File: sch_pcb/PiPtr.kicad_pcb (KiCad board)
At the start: 2 copper layers, 101.6 x 152.4 mm, 318 parts, among them J101 GLOBAL LINK 1 LEFT, J102 GLOBAL LINK 1 RIGHT, J104 GLOBAL LINK 2 LEFT, J106 GLOBAL LINK 2 RIGHT, J107 RASPBERRY_PI, J111 FP_PIXEL, J112 AM2302, J113 I2C1_5V, J114 I2C0_3v3, J117 OLED, J201 TO_SOUNDCARD, J202 FROM_SOUNDCARD, J203 Radio Port, J204 DB9_FEMALE, J301 SPARE, J302 SPARE, J303 SPARE, J304 SPARE, J305 USER_GPIO, J306 SPARE, J307 SPARE, J308 SPARE, J309 SPARE, J310 SPARE, J311 SPARE, J312 USER_ADC, J313 SPARE, J314 SPARE, J315 12VDC_IN, J401 TO_SOUNDCARD, J402 FROM_SOUNDCARD, J403 Radio Port, J404 DB9_FEMALE, Q101 2N7000, Q102 2N7000, Q103 2N7000, Q104 2N7000, Q105 2N7000, Q201 2N7000, Q202 2N7000, Q203 2N7000, Q301 SPARE, Q302 SPARE, Q401 2N7000, Q402 2N7000, Q403 2N7000, U101 MCP23017, U102 IP4234CZ6, U103 MCP4351, U104 74HC138, U105 74LVC1G125, U106 MCP4351, U107 MCP4351, U108 IP4234CZ6, U109 IP4234CZ6, U110 CD4050B, U201 MCP6004N, U202 74LVC1G3157, U203 74LVC1G3157, U204 74LVC4066, U205 MCP6004N, U206 74LVC1G3157, U207 MCP6S26, U301 MCP23017, U302 SPARE, U303 SPARE, U304 MCP3008, U305 MCP1703A-2502/MB, U306 TPS54302, U401 MCP6004N, U402 74LVC1G3157, U403 74LVC1G3157, U404 74LVC4066, U405 MCP6004N, U406 74LVC1G3157, U407 MCP6S26

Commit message: Updates based on emails
Disconnect SDO on PGAs
Add mounting holes 
More placement on PCB - for now, delete all 4xx sheet footprints.  Once channel 1 is placed, it will get copied to make channel 2.
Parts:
- removed C401, C402, C404, C408, C414, C415, C416, C418, C421, C423, C424, C425: 4.7u, lib:smd0603
- removed C403, C411, C413, C417, C419: 33p, lib:smd0603
- removed C405, C407, C420, C422: 0.1u, lib:smd0603
- removed C409, C410: 0.027u, lib:smd0603
- removed C412: 0.0039u, lib:smd0603
- removed C426, C427, C428, C429, C430, C431: 100p, lib:smd0603
- removed Q401, Q402, Q403: 2N7000, lib:SOT23
- removed R401, R410, R427, R436, R437, R440: 100k, lib:smd0603
- removed R402, R403, R408, R413, R430, R438, R439: 1k, lib:smd0603
- removed R404, R420, R431, R441, R442, R443: 20k, lib:smd0603
- removed R405, R406, R421, R422, R424, R425, R428, R429, R432, R433: 10k, lib:smd0603
- removed R407, R411, R434: 33, lib:smd0603
- removed R412, R415, R419, R426: 2k, lib:smd0603
- removed R414: 13k7, lib:smd0603
- removed R416, R418: 50k, lib:smd0603
- removed R417: 27k, lib:smd0603
- removed R423: 200k, lib:smd0603
- removed R435: 680, lib:smd0603
- removed TP401: TESTPOINT, lib:Wire_28AWG
- removed U401, U405: MCP6004N, lib:SOIC14
- removed U402, U403, U406: 74LVC1G3157, lib:SOT23-6
- removed U404: 74LVC4066, lib:SOIC14
- removed U407: MCP6S26, lib:SOIC14
- added MTG301: VAL**, lib:MTG_4_40, F.Cu at (59.7, 31.8)
- C311, C312, C313, C314, C315, C316, C317, C318: footprint lib:smd0805 -> lib:smd0603
- U301: moved to B.Cu
- moved U109 275.8 mm to (44.5, 190.5), turned to 90 degrees
- moved J113 262.8 mm to (25.4, 186.7)
- moved J114 262.8 mm to (41.9, 186.7)
- moved U108 254.6 mm to (27.9, 189.9), turned to 90 degrees
- moved TP104 246.7 mm to (24.1, 189.9)
- moved J102 231.8 mm to (39.4, 153.0)
- moved TP105 230.1 mm to (40.6, 189.9)
- moved J101 226.7 mm to (40.0, 142.9)
- moved U104 224.8 mm to (23.5, 149.2)
- moved U110 224.8 mm to (23.5, 157.5)
- moved C209 224.7 mm to (19.7, 109.9)
- moved C211 224.7 mm to (19.7, 119.4)
- moved C213 224.7 mm to (19.7, 117.5)
- moved R214 224.7 mm to (19.7, 108.0)
- moved R216 224.7 mm to (19.7, 111.8)
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
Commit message: Add files via upload
Fix missing pin numbers on opamps
Change two 4.7uF caps in parallel to 10uF/0805.  This will save 6 caps and will handle capacitance loss due to DC bias better
Change 2 22uF caps to 4 10uF caps to get rid of an extra BOM line item
More work on placement.  The channel now fits in the space allocated to it. 
Connectors need to be revisited - GPIO and soundcard
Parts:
- removed C215, C218, C224, C406: 4.7u, lib:smd0603
- removed J403: Radio Port, lib:RibbonHeader2x5
- added MTG302: VAL**, lib:MTG_4_40, F.Cu at (59.4, 176.8)
- added MTG303: VAL**, lib:MTG_4_40, F.Cu at (154.2, 177.0)
- added MTG304: VAL**, lib:MTG_4_40, F.Cu at (153.9, 31.5)
- U301: moved to F.Cu
- moved R122 160.1 mm to (178.3, 123.7)
- moved J401 152.5 mm to (112.5, 210.3), turned to 180 degrees
- moved J402 149.9 mm to (129.3, 211.3), turned to 180 degrees
- moved J404 108.3 mm to (113.5, 43.9)
- moved U107 106.7 mm to (174.2, 80.3), turned to 270 degrees
- moved J311 95.6 mm to (83.8, 90.2), turned to 90 degrees
- moved R227 93.8 mm to (89.4, 52.8)
- moved J102 93.2 mm to (130.3, 173.5), turned to 180 degrees
- moved J308 83.8 mm to (96.0, 90.7), turned to 90 degrees
- moved R203 75.1 mm to (82.3, 106.4)
- moved R204 71.9 mm to (82.0, 109.0)
- moved C216 71.3 mm to (89.4, 51.3)
- moved U110 69.6 mm to (81.8, 119.4)
- moved C220 68.8 mm to (77.2, 68.6), turned to 180 degrees
- moved C211 67.8 mm to (80.8, 89.9), turned to 90 degrees
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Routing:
- net /CH1/TX_CTCSS: track 0.00 -> 45.7 mm
- net /CH1/TX_AUDIO: track 0.00 -> 21.9 mm
- net /CH1/PTT: track 0.00 -> 10.0 mm
- net /CH1/RX_COR: track 0.00 -> 9.77 mm
- net /CH1/RX_AUDIO: track 0.00 -> 9.67 mm
- net /CH1/RX_CTCSS: track 0.00 -> 9.41 mm
- net /CH1/VDDA_2: track 0.00 -> 5.85 mm
- net Net-(C214-Pad2): track 0.00 -> 5.70 mm
- net Net-(C219-Pad1): track 0.00 -> 5.56 mm
- net Net-(C217-Pad2): track 0.00 -> 5.33 mm
- net Net-(C203-Pad2): track 0.00 -> 5.33 mm
- net Net-(C223-Pad2): track 0.00 -> 5.31 mm
- net Net-(C225-Pad1): track 0.00 -> 5.20 mm
- net Net-(C219-Pad2): track 0.00 -> 4.85 mm
- net Net-(C203-Pad1): track 0.00 -> 3.91 mm
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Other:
- board text added: "ADC/GPIO"
- board text added: "CHAN 1"
- board text added: "CHAN 2"
- board text added: "Todo: Replace with Molex/JST"

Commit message: Add files via upload
Changed  user_adc connector to 2x7 (14-pin is a lot more common than 12-pin)
Changed user_gpio connector to 2 2x8 connectors.  1x20 takes too much linear space
First pass layout on the two audio channels.  Right now, board is 4-layer, 100x150mm.  May be able to knock down the 150mm dimension 
The link and soundcard connectors fit in a row across the front edge.
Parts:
- removed J312: USER_ADC, lib:pin_array_6x2
- removed TP101: TESTPOINT, lib:Wire_28AWG
- added C324: 10u, lib:smd0805, F.Cu at (89.2, 226.1)
- added C325: 10u, lib:smd0805, F.Cu at (93.2, 230.6)
- added C401: 4.7u, lib:smd0603, F.Cu at (125.7, 55.9)
- added C402: 4.7u, lib:smd0603, F.Cu at (102.9, 86.6)
- added C403: 33p, lib:smd0603, F.Cu at (106.4, 56.4)
- added C404: 4.7u, lib:smd0603, F.Cu at (107.7, 90.2)
- added C405: 0.1u, lib:smd0603, F.Cu at (109.2, 90.2)
- added C406: 4.7u, lib:smd0603, F.Cu at (119.6, 55.9)
- added C407: 0.1u, lib:smd0603, F.Cu at (124.7, 73.2)
- added C408: 4.7u, lib:smd0603, F.Cu at (124.7, 71.6)
- added C409: 0.027u, lib:smd0603, F.Cu at (114.6, 83.8)
- added C410: 0.027u, lib:smd0603, F.Cu at (108.7, 94.0)
- added C411: 33p, lib:smd0603, F.Cu at (120.1, 84.6)
- added C412: 0.0039u, lib:smd0603, F.Cu at (117.9, 97.5)
- added C413: 33p, lib:smd0603, F.Cu at (110.7, 84.6)
- added C414: 10u, lib:smd0805, F.Cu at (116.3, 56.4)
- added C416: 10u, lib:smd0805, F.Cu at (120.4, 69.8)
- added C417: 33p, lib:smd0603, F.Cu at (113.0, 54.9)
- added C419: 33p, lib:smd0603, F.Cu at (114.3, 68.6)
- added C420: 0.1u, lib:smd0603, F.Cu at (110.5, 67.1)
- added C421: 4.7u, lib:smd0603, F.Cu at (110.5, 68.6)
- added C422: 0.1u, lib:smd0603, F.Cu at (103.6, 94.0)
- added C423: 10u, lib:smd0805, F.Cu at (104.9, 68.2)
- added C425: 4.7u, lib:smd0603, F.Cu at (108.2, 68.6)
- added C426: 100p, lib:smd0603, F.Cu at (119.0, 48.3)
- added C427: 100p, lib:smd0603, F.Cu at (117.3, 48.3)
- added C428: 100p, lib:smd0603, F.Cu at (113.3, 48.3)
- added C429: 100p, lib:smd0603, F.Cu at (110.7, 48.3)
- added C430: 100p, lib:smd0603, F.Cu at (107.6, 48.3)
- added C431: 100p, lib:smd0603, F.Cu at (114.6, 48.3)
- added J403: Radio Port, lib:RibbonHeader2x5, F.Cu at (113.3, 36.8)
- added Q401: 2N7000, lib:SOT23, F.Cu at (100.6, 49.5)
- added Q402: 2N7000, lib:SOT23, F.Cu at (100.6, 65.3)
- added Q403: 2N7000, lib:SOT23, F.Cu at (100.6, 57.7)
- added R121: 10k, lib:smd0603, F.Cu at (115.7, 62.4)
- added R401: 100k, lib:smd0603, F.Cu at (125.7, 54.4)
- added R402: 1k, lib:smd0603, F.Cu at (125.7, 57.4)
- added R403: 1k, lib:smd0603, F.Cu at (102.1, 94.0)
- added R404: 20k, lib:smd0603, F.Cu at (100.3, 94.0)
- added R405: 10k, lib:smd0603, F.Cu at (106.4, 54.9)
- added R406: 10k, lib:smd0603, F.Cu at (106.4, 53.3)
- added R407: 33, lib:smd0603, F.Cu at (106.2, 90.2)
- added R408: 1k, lib:smd0603, F.Cu at (115.1, 74.7)
- added R410: 100k, lib:smd0603, F.Cu at (121.2, 54.4)
- added R411: 33, lib:smd0603, F.Cu at (124.7, 70.1)
- added R412: 2k, lib:smd0603, F.Cu at (115.1, 76.2)
- added R413: 1k, lib:smd0603, F.Cu at (119.6, 57.4)
- added R414: 13k7, lib:smd0603, F.Cu at (108.7, 92.5)
- added R415: 2k, lib:smd0603, F.Cu at (115.1, 77.7)
- added R416: 50k, lib:smd0603, F.Cu at (113.8, 96.8)
- added R417: 27k, lib:smd0603, F.Cu at (108.7, 95.5)
- added R418: 50k, lib:smd0603, F.Cu at (119.4, 97.5)
- added R419: 2k, lib:smd0603, F.Cu at (115.1, 79.0)
- added R420: 20k, lib:smd0603, F.Cu at (117.3, 71.6)
- added R421: 10k, lib:smd0603, F.Cu at (120.1, 86.1)
- added R422: 10k, lib:smd0603, F.Cu at (122.4, 85.3)
- added R423: 200k, lib:smd0603, F.Cu at (116.3, 97.5)
- added R424: 10k, lib:smd0603, F.Cu at (112.3, 84.6)
- added R425: 10k, lib:smd0603, F.Cu at (108.2, 87.9)
- added R426: 2k, lib:smd0603, F.Cu at (115.1, 80.5)
- added R427: 100k, lib:smd0603, F.Cu at (120.4, 71.4)
- added R428: 10k, lib:smd0603, F.Cu at (113.0, 56.4)
- added R429: 10k, lib:smd0603, F.Cu at (113.0, 53.3)
- added R430: 1k, lib:smd0603, F.Cu at (120.4, 68.3)
- added R431: 20k, lib:smd0603, F.Cu at (115.1, 70.9)
- added R432: 10k, lib:smd0603, F.Cu at (114.3, 67.1)
- added R433: 10k, lib:smd0603, F.Cu at (113.5, 70.9)
- added R434: 33, lib:smd0603, F.Cu at (110.5, 70.1)
- added R435: 680, lib:smd0603, F.Cu at (87.0, 220.9)
- added R436: 100k, lib:smd0603, F.Cu at (104.4, 70.9)
- added R437: 100k, lib:smd0603, F.Cu at (106.7, 68.6)
- added R438: 1k, lib:smd0603, F.Cu at (100.3, 53.3)
- added R439: 1k, lib:smd0603, F.Cu at (100.1, 62.5)
- added R440: 100k, lib:smd0603, F.Cu at (103.9, 64.9)
- added R441: 20k, lib:smd0603, F.Cu at (100.1, 61.0)
- added R442: 20k, lib:smd0603, F.Cu at (100.3, 54.9)
- added R443: 20k, lib:smd0603, F.Cu at (103.1, 68.6)
- added TP301: TESTPOINT, lib:Wire_28AWG, F.Cu at (91.2, 96.5)
- added TP302: TESTPOINT, lib:Wire_28AWG, F.Cu at (91.2, 98.6)
- added TP303: TESTPOINT, lib:Wire_28AWG, F.Cu at (91.2, 100.6)
- added TP304, TP305, TP306: TESTPOINT, lib:Wire_28AWG, F.Cu at (87.0, 220.9)
- added TP401: TESTPOINT, lib:Wire_28AWG, F.Cu at (104.4, 51.3)
- added U111: 74LV1T125, lib:SOT23-5, F.Cu at (62.7, 230.6)
- added U112: 74LV1T125, lib:SOT23-5, F.Cu at (56.1, 230.1)
- added U401: MCP6004N, lib:SOIC14, F.Cu at (114.6, 90.9)
- added U402: 74LVC1G3157, lib:SOT23-6, F.Cu at (106.9, 85.3)
- added U403: 74LVC1G3157, lib:SOT23-6, F.Cu at (102.6, 90.4)
- added U404: 74LVC4066, lib:SOIC14, F.Cu at (105.7, 78.2)
- added U405: MCP6004N, lib:SOIC14, F.Cu at (109.7, 61.5)
- added U406: 74LVC1G3157, lib:SOT23-6, F.Cu at (123.2, 97.5)
- added U407: MCP6S26, lib:SOIC14, F.Cu at (120.9, 78.7)
- C214, C216, C223: value 4.7u -> 10u; footprint lib:smd0603 -> lib:smd0805
- C322, C323: value 22u -> 10u
- J305: value USER_GPIO -> USER_GPIO_2; footprint lib:SIL-20 -> lib:RibbonHeader2x8
- J308: value SPARE -> USER_GPIO_1; footprint lib:SIL-3 -> lib:RibbonHeader2x8
- J311: value SPARE -> USER_ADC; footprint lib:SIL-3 -> lib:RibbonHeader2x7
- MTG301, MTG302, MTG303, MTG304: value VAL** -> MOUNTING_HOLE
- U105: value 74LVC1G125 -> 74LV1T125
- moved J313 305.0 mm to (12.7, 221.0)
- moved J302 297.2 mm to (12.7, 228.6)
- moved J314 292.4 mm to (12.7, 217.2)
- moved U302 280.3 mm to (34.3, 224.8)
- moved J111 246.0 mm to (34.3, 218.4)
- moved Q301 242.5 mm to (78.0, 227.1), turned to 0 degrees
- moved J303 236.7 mm to (75.4, 212.9)
- moved Q302 235.3 mm to (73.4, 227.1), turned to 0 degrees
- moved R306 232.0 mm to (87.0, 220.9), turned to 0 degrees
- moved J304 231.7 mm to (75.4, 215.9)
- moved R303 228.0 mm to (87.0, 220.9), turned to 0 degrees
- moved R305 227.0 mm to (87.0, 220.9), turned to 0 degrees
- moved U306 224.8 mm to (62.7, 223.5)
- moved R302 223.5 mm to (87.0, 220.9), turned to 0 degrees
- moved R307 222.8 mm to (87.0, 220.9), turned to 0 degrees
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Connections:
- J107 pad 10: /UINTB -> /UINTB_33
- J107 pad 8: /UINTA -> /UINTA_33
- J305 pad 1: GND -> Net-(J305-Pad1)
- J305 pad 10: Net-(J305-Pad10) -> GND
- J305 pad 11: GND -> Net-(J305-Pad11)
- J305 pad 12: Net-(J305-Pad12) -> GND
- J305 pad 14: Net-(J305-Pad14) -> GND
- J305 pad 16: Net-(J305-Pad16) -> GND
- J305 pad 4: Net-(J305-Pad4) -> GND
- J305 pad 6: Net-(J305-Pad6) -> GND
- J305 pad 8: Net-(J305-Pad8) -> GND
- J308 pad 2: Net-(J308-Pad2) -> GND
- J311 pad 1: Net-(J311-Pad1) -> /Spares, GPIO, and ADC/ADC0
- J311 pad 2: Net-(J311-Pad2) -> GND
- J311 pad 3: Net-(J311-Pad3) -> /Spares, GPIO, and ADC/ADC1
- U101 pad 8: Net-(TP101-Pad1) -> /~UINT_ENA
- U106 pad 1: Net-(J311-Pad3) -> Net-(TP306-Pad1)
- U106 pad 18: Net-(J308-Pad1) -> Net-(TP301-Pad1)
- U106 pad 19: Net-(J308-Pad2) -> Net-(TP302-Pad1)
- U106 pad 2: Net-(J311-Pad2) -> Net-(TP305-Pad1)
- U106 pad 20: Net-(J308-Pad3) -> Net-(TP303-Pad1)
- U106 pad 3: Net-(J311-Pad1) -> Net-(TP304-Pad1)
- U107 pad 15: Net-(R119-Pad1) -> Net-(R121-Pad1)
- U204 pad 10: Net-(R226-Pad2) -> Net-(R215-Pad2)
- U204 pad 12: /RX1_BUS3_EN -> /RX1_BUS1_EN
- U204 pad 13: /RX1_LOCAL_EN -> /RX1_BUS2_EN
- U204 pad 2: Net-(R212-Pad2) -> Net-(R219-Pad2)
- U204 pad 3: Net-(R215-Pad2) -> Net-(R226-Pad2)
- U204 pad 5: /RX1_BUS1_EN -> /RX1_BUS3_EN
- U204 pad 6: /RX1_BUS2_EN -> /RX1_LOCAL_EN
- U204 pad 9: Net-(R219-Pad2) -> Net-(R212-Pad2)
- U207 pad 12: MISO_5 -> (no net)
- U301 pad 1: Net-(J305-Pad3) -> Net-(J305-Pad1)
- U301 pad 19: /UINTB -> /UINTB_5
- U301 pad 2: Net-(J305-Pad4) -> Net-(J305-Pad3)
- U301 pad 20: /UINTA -> /UINTA_5
- U301 pad 21: Net-(J305-Pad12) -> Net-(J308-Pad1)
- U301 pad 22: Net-(J305-Pad13) -> Net-(J308-Pad3)
- U301 pad 23: Net-(J305-Pad14) -> Net-(J308-Pad5)
- U301 pad 24: Net-(J305-Pad15) -> Net-(J308-Pad7)
- U301 pad 25: Net-(J305-Pad16) -> Net-(J308-Pad9)
- U301 pad 26: Net-(J305-Pad17) -> Net-(J308-Pad11)
- U301 pad 27: Net-(J305-Pad18) -> Net-(J308-Pad13)
- U301 pad 28: Net-(J305-Pad19) -> Net-(J308-Pad15)
- U301 pad 4: Net-(J305-Pad6) -> Net-(J305-Pad7)
- U301 pad 5: Net-(J305-Pad7) -> Net-(J305-Pad9)
- U301 pad 6: Net-(J305-Pad8) -> Net-(J305-Pad11)
- U301 pad 7: Net-(J305-Pad9) -> Net-(J305-Pad13)
- U301 pad 8: Net-(J305-Pad10) -> Net-(J305-Pad15)
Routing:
- net +5V: track 0.00 -> 333.5 mm, vias 0 -> 21
- net SCLK_5: track 0.00 -> 123.5 mm, vias 0 -> 4
- net MISO_5: track 0.00 -> 118.2 mm, vias 0 -> 8
- net MOSI_5: track 0.00 -> 114.4 mm, vias 0 -> 6
- net GND: track 0.00 -> 78.7 mm, vias 0 -> 41
- net /CH2/RX_CTCSS: track 0.00 -> 64.5 mm, vias 0 -> 1
- net Net-(C403-Pad1): track 0.00 -> 63.3 mm, vias 0 -> 4
- net /CH1/RX_CTCSS: track 9.41 -> 64.5 mm, vias 0 -> 1
- net /PTT2D: track 0.00 -> 53.3 mm
- net /PTT1D: track 0.00 -> 53.3 mm
- net +2V5: track 0.00 -> 48.8 mm, vias 0 -> 34
- net Net-(U103-Pad12): track 0.00 -> 47.1 mm, vias 0 -> 2
- net /~CTCSS2: track 0.00 -> 46.4 mm
- net /~CTCSS1: track 0.00 -> 46.4 mm
- net /LINK2_AUD: track 0.00 -> 45.1 mm, vias 0 -> 2
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- added copper zone on In2.Cu, net +2V5
- added copper zone on In1.Cu, net GND
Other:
- board size 101.6 x 152.4 mm -> 105 x 150 mm
- copper layers 2 -> 4
- board text removed: "ADC/GPIO"
- board text removed: "Todo: Replace with Molex/JST"

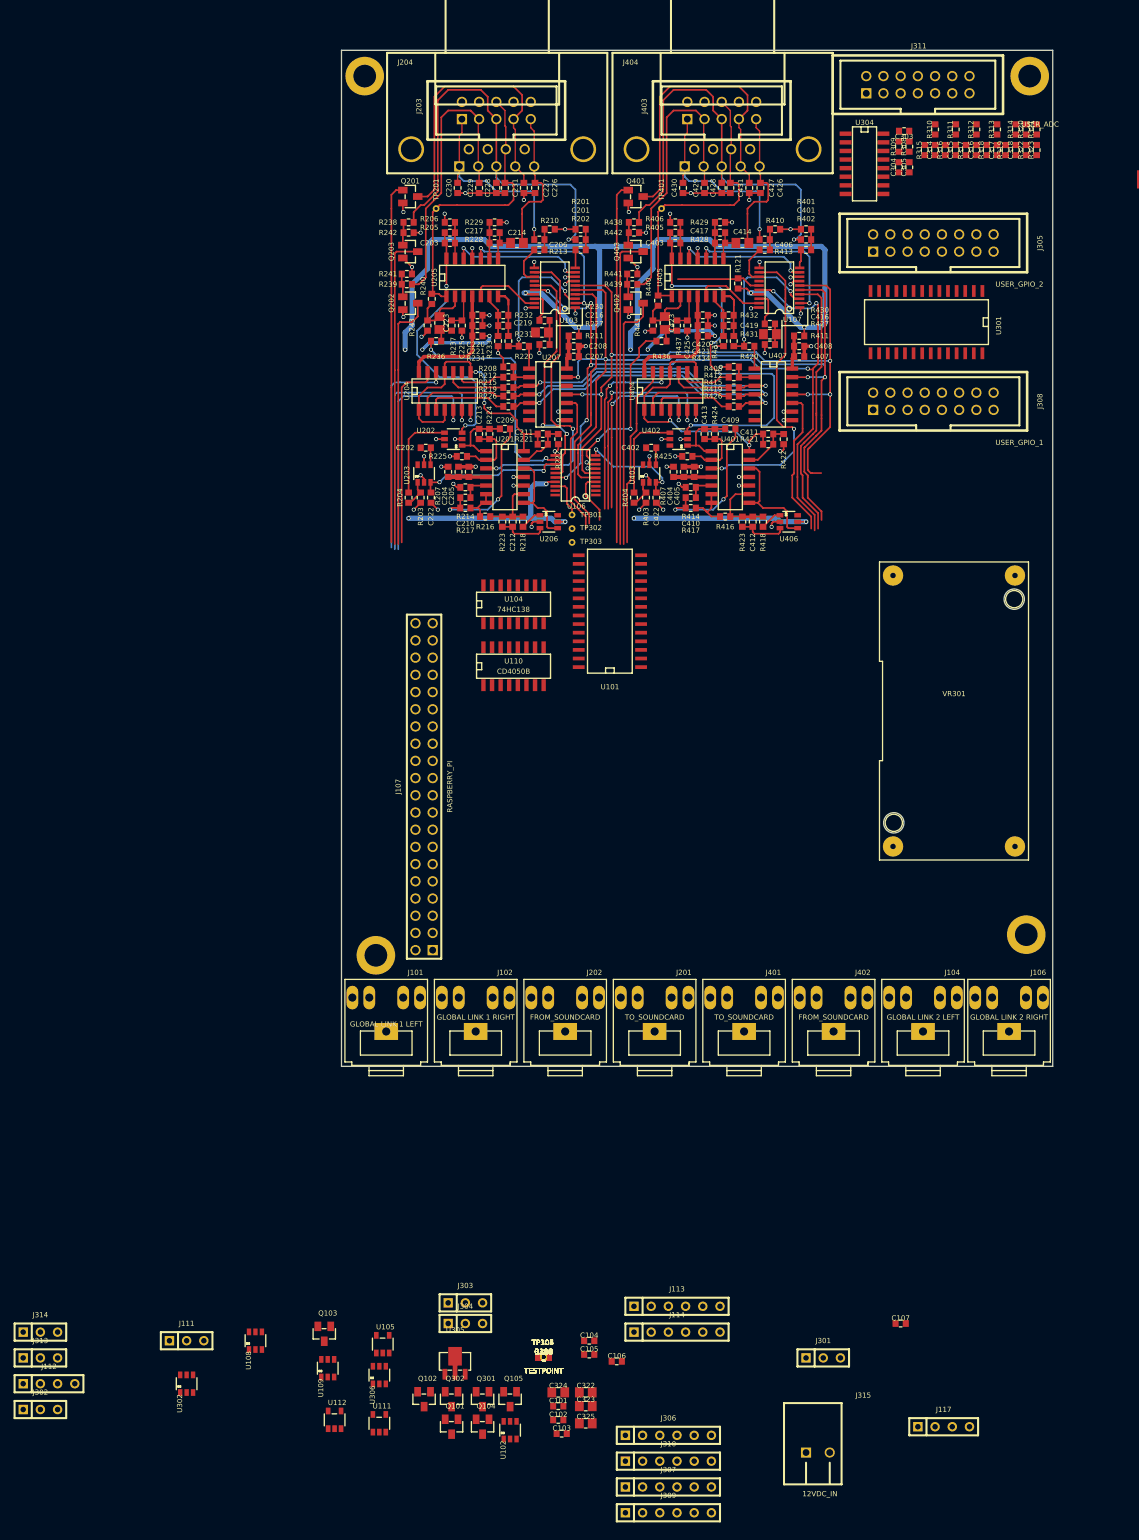
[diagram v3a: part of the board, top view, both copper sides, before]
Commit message: Add files via upload
Reversed ends on all pots so up increases level
Added outline and mounting holes to RasPi footprint so we can see how big it really is
Moved parts away from one of the RasPi mounting holes so we can use all 4 of them
More routing - finished user GPIO and ADC, SPI chipselect decoder
Still to do: level shifters, RasPi connections and spares
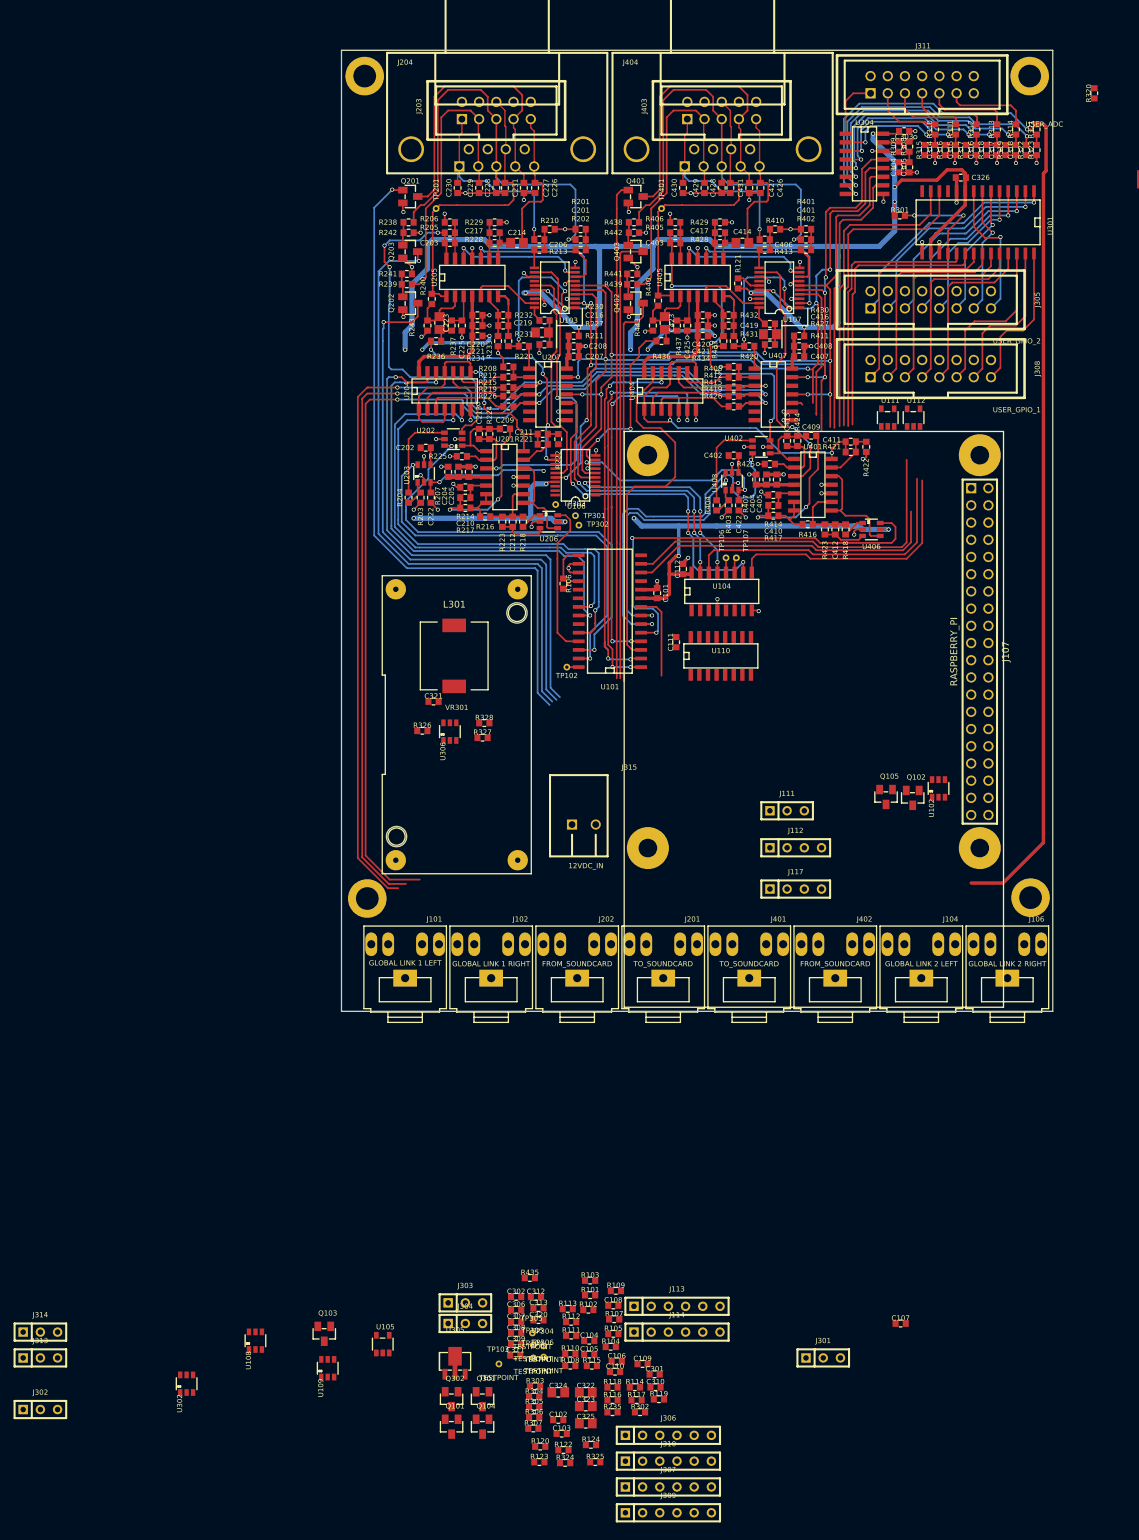
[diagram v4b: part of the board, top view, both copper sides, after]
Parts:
- added C326: 0.1u, lib:smd0603, F.Cu at (148.6, 46.7)
- added L301: 10uH, lib:Inductor_Wurth_7447714100, F.Cu at (73.8, 117.3)
- J107: footprint lib:PIN_ARRAY_20X2 -> lib:RaspberryPi2x20
- moved R301 176.6 mm to (139.6, 52.3)
- moved U112 170.9 mm to (141.6, 82.2)
- moved U111 166.4 mm to (137.8, 82.2)
- moved J112 135.7 mm to (124.2, 145.7)
- moved TP107 121.4 mm to (115.4, 102.9)
- moved TP106 121.0 mm to (113.9, 102.9)
- moved C101 120.9 mm to (103.8, 108.1), turned to 90 degrees
- moved J111 118.2 mm to (122.9, 140.2)
- moved C112 118.2 mm to (107.6, 104.5), turned to 90 degrees
- moved Q102 114.4 mm to (141.5, 138.3)
- moved R106 114.2 mm to (89.9, 106.7), turned to 270 degrees
- moved U102 113.9 mm to (145.3, 136.9)
- moved C111 107.4 mm to (106.6, 115.3), turned to 90 degrees
- moved Q105 104.8 mm to (137.5, 138.2)
- moved TP102 101.9 mm to (90.4, 119.0)
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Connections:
- U103 pad 1: +2V5 -> Net-(R220-Pad1)
- U103 pad 10: Net-(R202-Pad1) -> +2V5
- U103 pad 11: +2V5 -> Net-(R213-Pad1)
- U103 pad 13: Net-(R213-Pad1) -> +2V5
- U103 pad 18: /CH1/TONE_FROM_SOUNDCARD -> +2V5
- U103 pad 20: +2V5 -> /CH1/TONE_FROM_SOUNDCARD
- U103 pad 3: Net-(R220-Pad1) -> +2V5
- U103 pad 8: +2V5 -> Net-(R202-Pad1)
- U106 pad 10: /CH2/TONE_FROM_PI -> +2V5
- U106 pad 11: +2V5 -> /CH1/TONE_FROM_PI
- U106 pad 13: /CH1/TONE_FROM_PI -> +2V5
- U106 pad 8: +2V5 -> /CH2/TONE_FROM_PI
- U107 pad 1: +2V5 -> Net-(R420-Pad1)
- U107 pad 10: Net-(R402-Pad1) -> +2V5
- U107 pad 11: +2V5 -> Net-(R413-Pad1)
- U107 pad 13: Net-(R413-Pad1) -> +2V5
- U107 pad 18: /CH2/TONE_FROM_SOUNDCARD -> +2V5
- U107 pad 20: +2V5 -> /CH2/TONE_FROM_SOUNDCARD
- U107 pad 3: Net-(R420-Pad1) -> +2V5
- U107 pad 8: +2V5 -> Net-(R402-Pad1)
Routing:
- net +12V: track 0.00 -> 120.5 mm
- net /CH1/LOCAL_LINK: track 43.5 -> 150.8 mm, vias 2 -> 3
- net /LINK1_AUD: track 44.1 -> 149.5 mm, vias 2 -> 3
- net /LINK2_AUD: track 45.1 -> 150.2 mm, vias 2 -> 3
- net /SDA1_5: track 0.00 -> 99.7 mm
- net +5V: track 333.5 -> 431.3 mm, vias 21 -> 25
- net /SCL1_5: track 0.00 -> 93.5 mm
- net /RX1_DESC_EN: track 0.00 -> 65.5 mm, vias 0 -> 2
- net /RX2_DEEMP_EN: track 0.00 -> 63.2 mm, vias 0 -> 2
- net /PORT1_DET_EN: track 0.00 -> 61.0 mm, vias 0 -> 2
- net /RX2_DESC_EN: track 0.00 -> 55.4 mm, vias 0 -> 2
- net /RX1_BUS2_EN: track 28.4 -> 76.9 mm, vias 0 -> 1
- net /PTT1D: track 53.3 -> 100.6 mm, vias 0 -> 1
- net /COR1: track 37.8 -> 85.1 mm, vias 0 -> 1
- net /~CTCSS1: track 46.4 -> 93.4 mm, vias 0 -> 1
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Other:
- board size 105 x 150 mm -> 105 x 141.9 mm
- board text added: "LDR on front panel"
